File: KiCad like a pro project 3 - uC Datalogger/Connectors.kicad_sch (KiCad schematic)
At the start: 4 parts

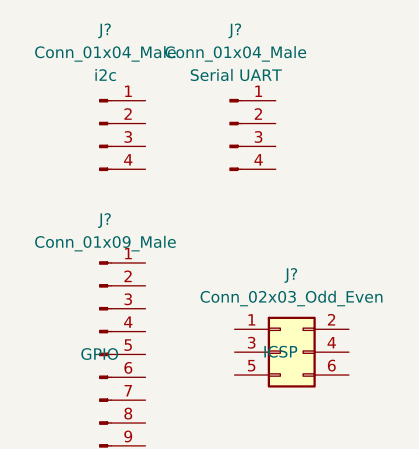
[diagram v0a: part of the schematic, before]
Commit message: changed locations of symbols (arrange)
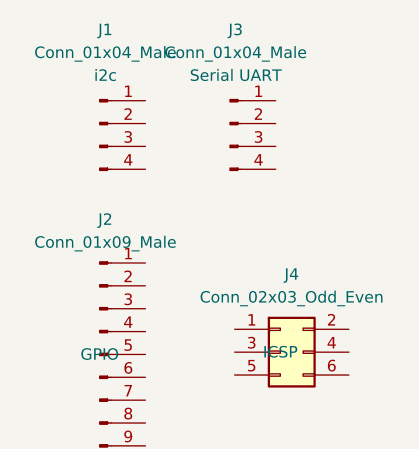
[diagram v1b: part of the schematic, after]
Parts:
- gave numbers to parts that had none: 4
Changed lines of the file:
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@@
   (symbol (lib_id "Connector_Generic:Conn_02x03_Odd_Even") (at 196.85 124.714 0) (unit 1)
     (in_bom yes) (on_board yes)
-    (property "Reference" "J?" (id 0) (at 198.12 116.078 0))
+    (property "Reference" "J4" (id 0) (at 198.12 116.078 0))
     (property "Value" "Conn_02x03_Odd_Even" (id 1) (at 198.12 118.618 0))
     (property "Footprint" "" (id 2) (at 196.85 124.714 0)
@@
   (symbol (lib_id "Connector:Conn_01x09_Male") (at 176.784 124.968 0) (unit 1)
     (in_bom yes) (on_board yes) (fields_autoplaced)
-    (property "Reference" "J?" (id 0) (at 177.419 109.982 0))
+    (property "Reference" "J2" (id 0) (at 177.419 109.982 0))
     (property "Value" "Conn_01x09_Male" (id 1) (at 177.419 112.522 0))
     (property "Footprint" "" (id 2) (at 176.784 124.968 0)
@@
   (symbol (lib_id "Connector:Conn_01x04_Male") (at 191.262 99.314 0) (unit 1)
     (in_bom yes) (on_board yes) (fields_autoplaced)
-    (property "Reference" "J?" (id 0) (at 191.897 88.9 0))
+    (property "Reference" "J3" (id 0) (at 191.897 88.9 0))
     (property "Value" "Conn_01x04_Male" (id 1) (at 191.897 91.44 0))
     (property "Footprint" "" (id 2) (at 191.262 99.314 0)
@@
   (symbol (lib_id "Connector:Conn_01x04_Male") (at 176.784 99.314 0) (unit 1)
     (in_bom yes) (on_board yes) (fields_autoplaced)
-    (property "Reference" "J?" (id 0) (at 177.419 88.9 0))
+    (property "Reference" "J1" (id 0) (at 177.419 88.9 0))
     (property "Value" "Conn_01x04_Male" (id 1) (at 177.419 91.44 0))
     (property "Footprint" "" (id 2) (at 176.784 99.314 0)

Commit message: completed symbol to footprint associations
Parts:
- J1, J3: footprint (none) -> Connector_PinHeader_2.54mm:PinHeader_1x04_P2.54mm_Vertical
- J2: footprint (none) -> Connector_PinHeader_2.54mm:PinHeader_1x09_P2.54mm_Vertical
- J4: footprint (none) -> Connector_PinHeader_2.54mm:PinHeader_2x03_P2.54mm_Vertical
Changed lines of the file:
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@@
     (property "Reference" "J4" (id 0) (at 198.12 116.078 0))
     (property "Value" "Conn_02x03_Odd_Even" (id 1) (at 198.12 118.618 0))
-    (property "Footprint" "" (id 2) (at 196.85 124.714 0)
+    (property "Footprint" "Connector_PinHeader_2.54mm:PinHeader_2x03_P2.54mm_Vertical" (id 2) (at 196.85 124.714 0)
       (effects (font (size 1.27 1.27)) hide)
     )
@@
     (property "Reference" "J2" (id 0) (at 177.419 109.982 0))
     (property "Value" "Conn_01x09_Male" (id 1) (at 177.419 112.522 0))
-    (property "Footprint" "" (id 2) (at 176.784 124.968 0)
+    (property "Footprint" "Connector_PinHeader_2.54mm:PinHeader_1x09_P2.54mm_Vertical" (id 2) (at 176.784 124.968 0)
       (effects (font (size 1.27 1.27)) hide)
     )
@@
     (property "Reference" "J3" (id 0) (at 191.897 88.9 0))
     (property "Value" "Conn_01x04_Male" (id 1) (at 191.897 91.44 0))
-    (property "Footprint" "" (id 2) (at 191.262 99.314 0)
+    (property "Footprint" "Connector_PinHeader_2.54mm:PinHeader_1x04_P2.54mm_Vertical" (id 2) (at 191.262 99.314 0)
       (effects (font (size 1.27 1.27)) hide)
     )
@@
     (property "Reference" "J1" (id 0) (at 177.419 88.9 0))
     (property "Value" "Conn_01x04_Male" (id 1) (at 177.419 91.44 0))
-    (property "Footprint" "" (id 2) (at 176.784 99.314 0)
+    (property "Footprint" "Connector_PinHeader_2.54mm:PinHeader_1x04_P2.54mm_Vertical" (id 2) (at 176.784 99.314 0)
       (effects (font (size 1.27 1.27)) hide)
     )

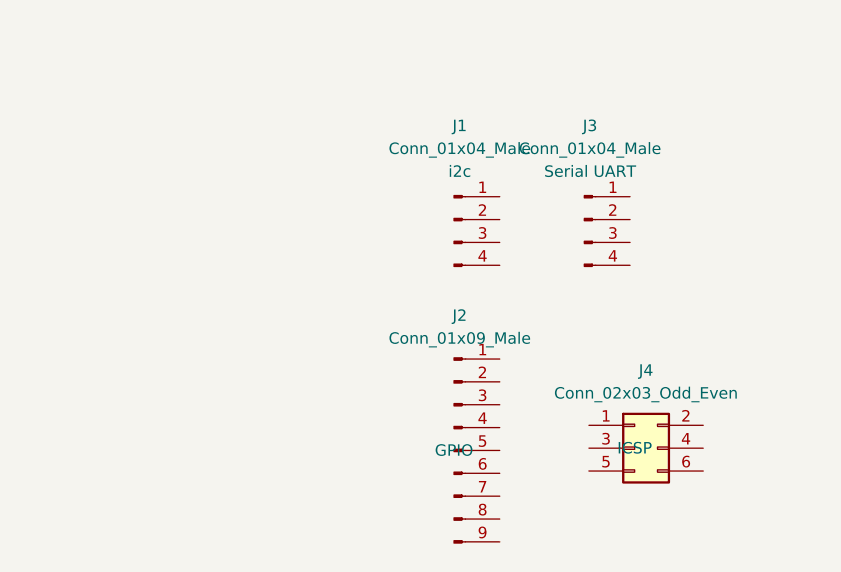
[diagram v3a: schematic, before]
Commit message: finished wiring on connector sheet
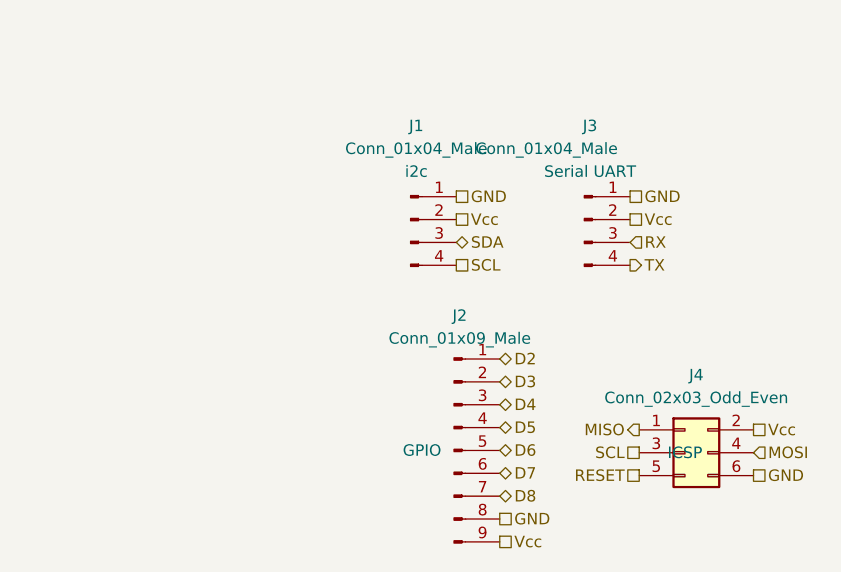
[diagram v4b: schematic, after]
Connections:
- net MISO: now reaches J4.1 (Pin_1)
- net Vcc: now reaches J4.2 (Pin_2)
- net Vcc: now also J1.2 (Pin_2), J2.9 (Pin_9), J3.2 (Pin_2)
- net SCL: now reaches J4.3 (Pin_3)
- net SCL: now also J1.4 (Pin_4)
- net MOSI: now reaches J4.4 (Pin_4)
- net RESET: now reaches J4.5 (Pin_5)
- net GND: now reaches J4.6 (Pin_6)
- net GND: now also J1.1 (Pin_1), J2.8 (Pin_8), J3.1 (Pin_1)
- net D2: now reaches J2.1 (Pin_1)
- net D3: now reaches J2.2 (Pin_2)
- net D4: now reaches J2.3 (Pin_3)
- net D5: now reaches J2.4 (Pin_4)
- net D6: now reaches J2.5 (Pin_5)
- net D7: now reaches J2.6 (Pin_6)
- net D8: now reaches J2.7 (Pin_7)
- net RX: now reaches J3.3 (Pin_3)
- net TX: now reaches J3.4 (Pin_4)
- net SDA: now reaches J1.3 (Pin_3)
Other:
- moved on the sheet: J1, J4
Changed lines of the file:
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@@
 (kicad_sch (version 20211123) (generator eeschema)
   (paper "A4")
-  (symbol (lib_id "Connector_Generic:Conn_02x03_Odd_Even") (at 196.85 124.714 0) (unit 1)
+  (hierarchical_label "D7" (shape bidirectional) (at 181.864 127.508 0)
+    (effects (font (size 1.27 1.27)) (justify left))
+  )
+  (hierarchical_label "RESET" (shape passive) (at 197.358 127.762 180)
+    (effects (font (size 1.27 1.27)) (justify right))
+  )
+  (hierarchical_label "RX" (shape input) (at 196.342 101.854 0)
+    (effects (font (size 1.27 1.27)) (justify left))
+  )
+  (hierarchical_label "TX" (shape output) (at 196.342 104.394 0)
+    (effects (font (size 1.27 1.27)) (justify left))
+  )
+  (hierarchical_label "SCL" (shape passive) (at 177.038 104.394 0)
+    (effects (font (size 1.27 1.27)) (justify left))
+  )
+  (hierarchical_label "D5" (shape bidirectional) (at 181.864 122.428 0)
+    (effects (font (size 1.27 1.27)) (justify left))
+  )
+  (hierarchical_label "D4" (shape bidirectional) (at 181.864 119.888 0)
+    (effects (font (size 1.27 1.27)) (justify left))
+  )
+  (hierarchical_label "SDA" (shape bidirectional) (at 177.038 101.854 0)
+    (effects (font (size 1.27 1.27)) (justify left))
+  )
+  (hierarchical_label "GND" (shape passive) (at 196.342 96.774 0)
+    (effects (font (size 1.27 1.27)) (justify left))
+  )
+  (hierarchical_label "GND" (shape passive) (at 177.038 96.774 0)
+    (effects (font (size 1.27 1.27)) (justify left))
+  )
+  (hierarchical_label "D8" (shape bidirectional) (at 181.864 130.048 0)
+    (effects (font (size 1.27 1.27)) (justify left))
+  )
+  (hierarchical_label "SCL" (shape passive) (at 197.358 125.222 180)
+    (effects (font (size 1.27 1.27)) (justify right))
+  )
+  (hierarchical_label "GND" (shape passive) (at 181.864 132.588 0)
+    (effects (font (size 1.27 1.27)) (justify left))
+  )
+  (hierarchical_label "Vcc" (shape passive) (at 196.342 99.314 0)
+    (effects (font (size 1.27 1.27)) (justify left))
+  )
+  (hierarchical_label "Vcc" (shape passive) (at 210.058 122.682 0)
+    (effects (font (size 1.27 1.27)) (justify left))
+  )
+  (hierarchical_label "Vcc" (shape passive) (at 177.038 99.314 0)
+    (effects (font (size 1.27 1.27)) (justify left))
+  )
+  (hierarchical_label "GND" (shape passive) (at 210.058 127.762 0)
+    (effects (font (size 1.27 1.27)) (justify left))
+  )
+  (hierarchical_label "MISO" (shape output) (at 197.358 122.682 180)
+    (effects (font (size 1.27 1.27)) (justify right))
+  )
+  (hierarchical_label "D3" (shape bidirectional) (at 181.864 117.348 0)
+    (effects (font (size 1.27 1.27)) (justify left))
+  )
+  (hierarchical_label "Vcc" (shape passive) (at 181.864 135.128 0)
+    (effects (font (size 1.27 1.27)) (justify left))
+  )
+  (hierarchical_label "D2" (shape bidirectional) (at 181.864 114.808 0)
+    (effects (font (size 1.27 1.27)) (justify left))
+  )
+  (hierarchical_label "D6" (shape bidirectional) (at 181.864 124.968 0)
+    (effects (font (size 1.27 1.27)) (justify left))
+  )
+  (hierarchical_label "MOSI" (shape input) (at 210.058 125.222 0)
+    (effects (font (size 1.27 1.27)) (justify left))
+  )
+  (symbol (lib_id "Connector_Generic:Conn_02x03_Odd_Even") (at 202.438 125.222 0) (unit 1)
     (in_bom yes) (on_board yes)
-    (property "Reference" "J4" (id 0) (at 198.12 116.078 0))
-    (property "Value" "Conn_02x03_Odd_Even" (id 1) (at 198.12 118.618 0))
-    (property "Footprint" "Connector_PinHeader_2.54mm:PinHeader_2x03_P2.54mm_Vertical" (id 2) (at 196.85 124.714 0)
+    (property "Reference" "J4" (id 0) (at 203.708 116.586 0))
+    (property "Value" "Conn_02x03_Odd_Even" (id 1) (at 203.708 119.126 0))
+    (property "Footprint" "Connector_PinHeader_2.54mm:PinHeader_2x03_P2.54mm_Vertical" (id 2) (at 202.438 125.222 0)
       (effects (font (size 1.27 1.27)) hide)
     )
-    (property "Datasheet" "~" (id 3) (at 196.85 124.714 0)
+    (property "Datasheet" "~" (id 3) (at 202.438 125.222 0)
       (effects (font (size 1.27 1.27)) hide)
     )
-    (property "Purpose" "ICSP" (id 4) (at 196.85 124.714 0))
+    (property "Purpose" "ICSP" (id 4) (at 202.438 125.222 0))
     (pin "1")
     (pin "2")
@@
   )
   (symbol (lib_id "Connector:Conn_01x09_Male") (at 176.784 124.968 0) (unit 1)
-    (in_bom yes) (on_board yes) (fields_autoplaced)
+    (in_bom yes) (on_board yes)
     (property "Reference" "J2" (id 0) (at 177.419 109.982 0))
     (property "Value" "Conn_01x09_Male" (id 1) (at 177.419 112.522 0))
@@
       (effects (font (size 1.27 1.27)) hide)
     )
-    (property "Purpose" "GPIO" (id 4) (at 176.784 124.968 0))
+    (property "Purpose" "GPIO" (id 4) (at 173.228 124.968 0))
     (pin "1")
     (pin "2")
@@
   )
   (symbol (lib_id "Connector:Conn_01x04_Male") (at 191.262 99.314 0) (unit 1)
-    (in_bom yes) (on_board yes) (fields_autoplaced)
+    (in_bom yes) (on_board yes)
     (property "Reference" "J3" (id 0) (at 191.897 88.9 0))
-    (property "Value" "Conn_01x04_Male" (id 1) (at 191.897 91.44 0))
+    (property "Value" "Conn_01x04_Male" (id 1) (at 187.071 91.44 0))
     (property "Footprint" "Connector_PinHeader_2.54mm:PinHeader_1x04_P2.54mm_Vertical" (id 2) (at 191.262 99.314 0)
       (effects (font (size 1.27 1.27)) hide)
@@
     (pin "4")
   )
-  (symbol (lib_id "Connector:Conn_01x04_Male") (at 176.784 99.314 0) (unit 1)
+  (symbol (lib_id "Connector:Conn_01x04_Male") (at 171.958 99.314 0) (unit 1)
     (in_bom yes) (on_board yes) (fields_autoplaced)
-    (property "Reference" "J1" (id 0) (at 177.419 88.9 0))
-    (property "Value" "Conn_01x04_Male" (id 1) (at 177.419 91.44 0))
-    (property "Footprint" "Connector_PinHeader_2.54mm:PinHeader_1x04_P2.54mm_Vertical" (id 2) (at 176.784 99.314 0)
+    (property "Reference" "J1" (id 0) (at 172.593 88.9 0))
+    (property "Value" "Conn_01x04_Male" (id 1) (at 172.593 91.44 0))
+    (property "Footprint" "Connector_PinHeader_2.54mm:PinHeader_1x04_P2.54mm_Vertical" (id 2) (at 171.958 99.314 0)
       (effects (font (size 1.27 1.27)) hide)
     )
-    (property "Datasheet" "~" (id 3) (at 176.784 99.314 0)
+    (property "Datasheet" "~" (id 3) (at 171.958 99.314 0)
       (effects (font (size 1.27 1.27)) hide)
     )
-    (property "Purpose" "i2c" (id 4) (at 177.419 93.98 0))
+    (property "Purpose" "i2c" (id 4) (at 172.593 93.98 0))
     (pin "1")
     (pin "2")

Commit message: enh layout and text schematic
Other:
- title: (none) -> Connectors
- moved on the sheet: J1, J2, J3, J4
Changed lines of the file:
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@@
 (kicad_sch (version 20211123) (generator eeschema)
   (paper "A4")
-  (hierarchical_label "D7" (shape bidirectional) (at 181.864 127.508 0)
+  (title_block
+    (title "Connectors")
+    (date "2022-07-31")
+    (rev "V1.0")
+    (comment 1 "Casper Tak")
+  )
+  (hierarchical_label "D7" (shape bidirectional) (at 147.32 116.84 0)
     (effects (font (size 1.27 1.27)) (justify left))
   )
-  (hierarchical_label "RESET" (shape passive) (at 197.358 127.762 180)
+  (hierarchical_label "RESET" (shape passive) (at 162.814 117.094 180)
     (effects (font (size 1.27 1.27)) (justify right))
   )
-  (hierarchical_label "RX" (shape input) (at 196.342 101.854 0)
+  (hierarchical_label "RX" (shape input) (at 161.798 91.186 0)
     (effects (font (size 1.27 1.27)) (justify left))
   )
-  (hierarchical_label "TX" (shape output) (at 196.342 104.394 0)
+  (hierarchical_label "TX" (shape output) (at 161.798 93.726 0)
     (effects (font (size 1.27 1.27)) (justify left))
   )
-  (hierarchical_label "SCL" (shape passive) (at 177.038 104.394 0)
+  (hierarchical_label "SCL" (shape passive) (at 142.494 93.726 0)
     (effects (font (size 1.27 1.27)) (justify left))
   )
-  (hierarchical_label "D5" (shape bidirectional) (at 181.864 122.428 0)
+  (hierarchical_label "D5" (shape bidirectional) (at 147.32 111.76 0)
     (effects (font (size 1.27 1.27)) (justify left))
   )
-  (hierarchical_label "D4" (shape bidirectional) (at 181.864 119.888 0)
+  (hierarchical_label "D4" (shape bidirectional) (at 147.32 109.22 0)
     (effects (font (size 1.27 1.27)) (justify left))
   )
-  (hierarchical_label "SDA" (shape bidirectional) (at 177.038 101.854 0)
+  (hierarchical_label "SDA" (shape bidirectional) (at 142.494 91.186 0)
     (effects (font (size 1.27 1.27)) (justify left))
   )
-  (hierarchical_label "GND" (shape passive) (at 196.342 96.774 0)
+  (hierarchical_label "GND" (shape passive) (at 161.798 86.106 0)
     (effects (font (size 1.27 1.27)) (justify left))
   )
-  (hierarchical_label "GND" (shape passive) (at 177.038 96.774 0)
+  (hierarchical_label "GND" (shape passive) (at 142.494 86.106 0)
     (effects (font (size 1.27 1.27)) (justify left))
   )
-  (hierarchical_label "D8" (shape bidirectional) (at 181.864 130.048 0)
+  (hierarchical_label "D8" (shape bidirectional) (at 147.32 119.38 0)
     (effects (font (size 1.27 1.27)) (justify left))
   )
-  (hierarchical_label "SCL" (shape passive) (at 197.358 125.222 180)
+  (hierarchical_label "SCL" (shape passive) (at 162.814 114.554 180)
     (effects (font (size 1.27 1.27)) (justify right))
   )
-  (hierarchical_label "GND" (shape passive) (at 181.864 132.588 0)
+  (hierarchical_label "GND" (shape passive) (at 147.32 121.92 0)
     (effects (font (size 1.27 1.27)) (justify left))
   )
-  (hierarchical_label "Vcc" (shape passive) (at 196.342 99.314 0)
+  (hierarchical_label "Vcc" (shape passive) (at 161.798 88.646 0)
     (effects (font (size 1.27 1.27)) (justify left))
   )
-  (hierarchical_label "Vcc" (shape passive) (at 210.058 122.682 0)
+  (hierarchical_label "Vcc" (shape passive) (at 175.514 112.014 0)
     (effects (font (size 1.27 1.27)) (justify left))
   )
-  (hierarchical_label "Vcc" (shape passive) (at 177.038 99.314 0)
+  (hierarchical_label "Vcc" (shape passive) (at 142.494 88.646 0)
     (effects (font (size 1.27 1.27)) (justify left))
   )
-  (hierarchical_label "GND" (shape passive) (at 210.058 127.762 0)
+  (hierarchical_label "GND" (shape passive) (at 175.514 117.094 0)
     (effects (font (size 1.27 1.27)) (justify left))
   )
-  (hierarchical_label "MISO" (shape output) (at 197.358 122.682 180)
+  (hierarchical_label "MISO" (shape output) (at 162.814 112.014 180)
     (effects (font (size 1.27 1.27)) (justify right))
   )
-  (hierarchical_label "D3" (shape bidirectional) (at 181.864 117.348 0)
+  (hierarchical_label "D3" (shape bidirectional) (at 147.32 106.68 0)
     (effects (font (size 1.27 1.27)) (justify left))
   )
-  (hierarchical_label "Vcc" (shape passive) (at 181.864 135.128 0)
+  (hierarchical_label "Vcc" (shape passive) (at 147.32 124.46 0)
     (effects (font (size 1.27 1.27)) (justify left))
   )
-  (hierarchical_label "D2" (shape bidirectional) (at 181.864 114.808 0)
+  (hierarchical_label "D2" (shape bidirectional) (at 147.32 104.14 0)
     (effects (font (size 1.27 1.27)) (justify left))
   )
-  (hierarchical_label "D6" (shape bidirectional) (at 181.864 124.968 0)
+  (hierarchical_label "D6" (shape bidirectional) (at 147.32 114.3 0)
     (effects (font (size 1.27 1.27)) (justify left))
   )
-  (hierarchical_label "MOSI" (shape input) (at 210.058 125.222 0)
+  (hierarchical_label "MOSI" (shape input) (at 175.514 114.554 0)
     (effects (font (size 1.27 1.27)) (justify left))
   )
-  (symbol (lib_id "Connector_Generic:Conn_02x03_Odd_Even") (at 202.438 125.222 0) (unit 1)
+  (symbol (lib_id "Connector_Generic:Conn_02x03_Odd_Even") (at 167.894 114.554 0) (unit 1)
     (in_bom yes) (on_board yes)
-    (property "Reference" "J4" (id 0) (at 203.708 116.586 0))
-    (property "Value" "Conn_02x03_Odd_Even" (id 1) (at 203.708 119.126 0))
-    (property "Footprint" "Connector_PinHeader_2.54mm:PinHeader_2x03_P2.54mm_Vertical" (id 2) (at 202.438 125.222 0)
+    (property "Reference" "J4" (id 0) (at 169.164 105.918 0))
+    (property "Value" "Conn_02x03_Odd_Even" (id 1) (at 169.164 108.458 0))
+    (property "Footprint" "Connector_PinHeader_2.54mm:PinHeader_2x03_P2.54mm_Vertical" (id 2) (at 167.894 114.554 0)
       (effects (font (size 1.27 1.27)) hide)
     )
-    (property "Datasheet" "~" (id 3) (at 202.438 125.222 0)
+    (property "Datasheet" "~" (id 3) (at 167.894 114.554 0)
       (effects (font (size 1.27 1.27)) hide)
     )
-    (property "Purpose" "ICSP" (id 4) (at 202.438 125.222 0))
+    (property "Purpose" "ICSP" (id 4) (at 167.894 114.554 0))
     (pin "1")
     (pin "2")
@@
     (pin "6")
   )
-  (symbol (lib_id "Connector:Conn_01x09_Male") (at 176.784 124.968 0) (unit 1)
+  (symbol (lib_id "Connector:Conn_01x09_Male") (at 142.24 114.3 0) (unit 1)
     (in_bom yes) (on_board yes)
-    (property "Reference" "J2" (id 0) (at 177.419 109.982 0))
-    (property "Value" "Conn_01x09_Male" (id 1) (at 177.419 112.522 0))
-    (property "Footprint" "Connector_PinHeader_2.54mm:PinHeader_1x09_P2.54mm_Vertical" (id 2) (at 176.784 124.968 0)
+    (property "Reference" "J2" (id 0) (at 142.875 99.314 0))
+    (property "Value" "Conn_01x09_Male" (id 1) (at 142.875 101.854 0))
+    (property "Footprint" "Connector_PinHeader_2.54mm:PinHeader_1x09_P2.54mm_Vertical" (id 2) (at 142.24 114.3 0)
       (effects (font (size 1.27 1.27)) hide)
     )
-    (property "Datasheet" "~" (id 3) (at 176.784 124.968 0)
+    (property "Datasheet" "~" (id 3) (at 142.24 114.3 0)
       (effects (font (size 1.27 1.27)) hide)
     )
-    (property "Purpose" "GPIO" (id 4) (at 173.228 124.968 0))
+    (property "Purpose" "GPIO" (id 4) (at 138.684 114.3 0))
     (pin "1")
     (pin "2")
@@
     (pin "9")
   )
-  (symbol (lib_id "Connector:Conn_01x04_Male") (at 191.262 99.314 0) (unit 1)
+  (symbol (lib_id "Connector:Conn_01x04_Male") (at 156.718 88.646 0) (unit 1)
     (in_bom yes) (on_board yes)
-    (property "Reference" "J3" (id 0) (at 191.897 88.9 0))
-    (property "Value" "Conn_01x04_Male" (id 1) (at 187.071 91.44 0))
-    (property "Footprint" "Connector_PinHeader_2.54mm:PinHeader_1x04_P2.54mm_Vertical" (id 2) (at 191.262 99.314 0)
+    (property "Reference" "J3" (id 0) (at 157.353 78.232 0))
+    (property "Value" "Conn_01x04_Male" (id 1) (at 152.527 80.772 0))
+    (property "Footprint" "Connector_PinHeader_2.54mm:PinHeader_1x04_P2.54mm_Vertical" (id 2) (at 156.718 88.646 0)
       (effects (font (size 1.27 1.27)) hide)
     )
-    (property "Datasheet" "~" (id 3) (at 191.262 99.314 0)
+    (property "Datasheet" "~" (id 3) (at 156.718 88.646 0)
       (effects (font (size 1.27 1.27)) hide)
     )
-    (property "Purpose" "Serial UART" (id 4) (at 191.897 93.98 0))
+    (property "Purpose" "Serial UART" (id 4) (at 157.353 83.312 0))
     (pin "1")
     (pin "2")
@@
     (pin "4")
   )
-  (symbol (lib_id "Connector:Conn_01x04_Male") (at 171.958 99.314 0) (unit 1)
+  (symbol (lib_id "Connector:Conn_01x04_Male") (at 137.414 88.646 0) (unit 1)
     (in_bom yes) (on_board yes) (fields_autoplaced)
-    (property "Reference" "J1" (id 0) (at 172.593 88.9 0))
-    (property "Value" "Conn_01x04_Male" (id 1) (at 172.593 91.44 0))
-    (property "Footprint" "Connector_PinHeader_2.54mm:PinHeader_1x04_P2.54mm_Vertical" (id 2) (at 171.958 99.314 0)
+    (property "Reference" "J1" (id 0) (at 138.049 78.232 0))
+    (property "Value" "Conn_01x04_Male" (id 1) (at 138.049 80.772 0))
+    (property "Footprint" "Connector_PinHeader_2.54mm:PinHeader_1x04_P2.54mm_Vertical" (id 2) (at 137.414 88.646 0)
       (effects (font (size 1.27 1.27)) hide)
     )
-    (property "Datasheet" "~" (id 3) (at 171.958 99.314 0)
+    (property "Datasheet" "~" (id 3) (at 137.414 88.646 0)
       (effects (font (size 1.27 1.27)) hide)
     )
-    (property "Purpose" "i2c" (id 4) (at 172.593 93.98 0))
+    (property "Purpose" "i2c" (id 4) (at 138.049 83.312 0))
     (pin "1")
     (pin "2")
